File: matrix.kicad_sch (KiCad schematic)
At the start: 285 parts, among them SW2 SW_SPDT, SW3 SW_SPDT

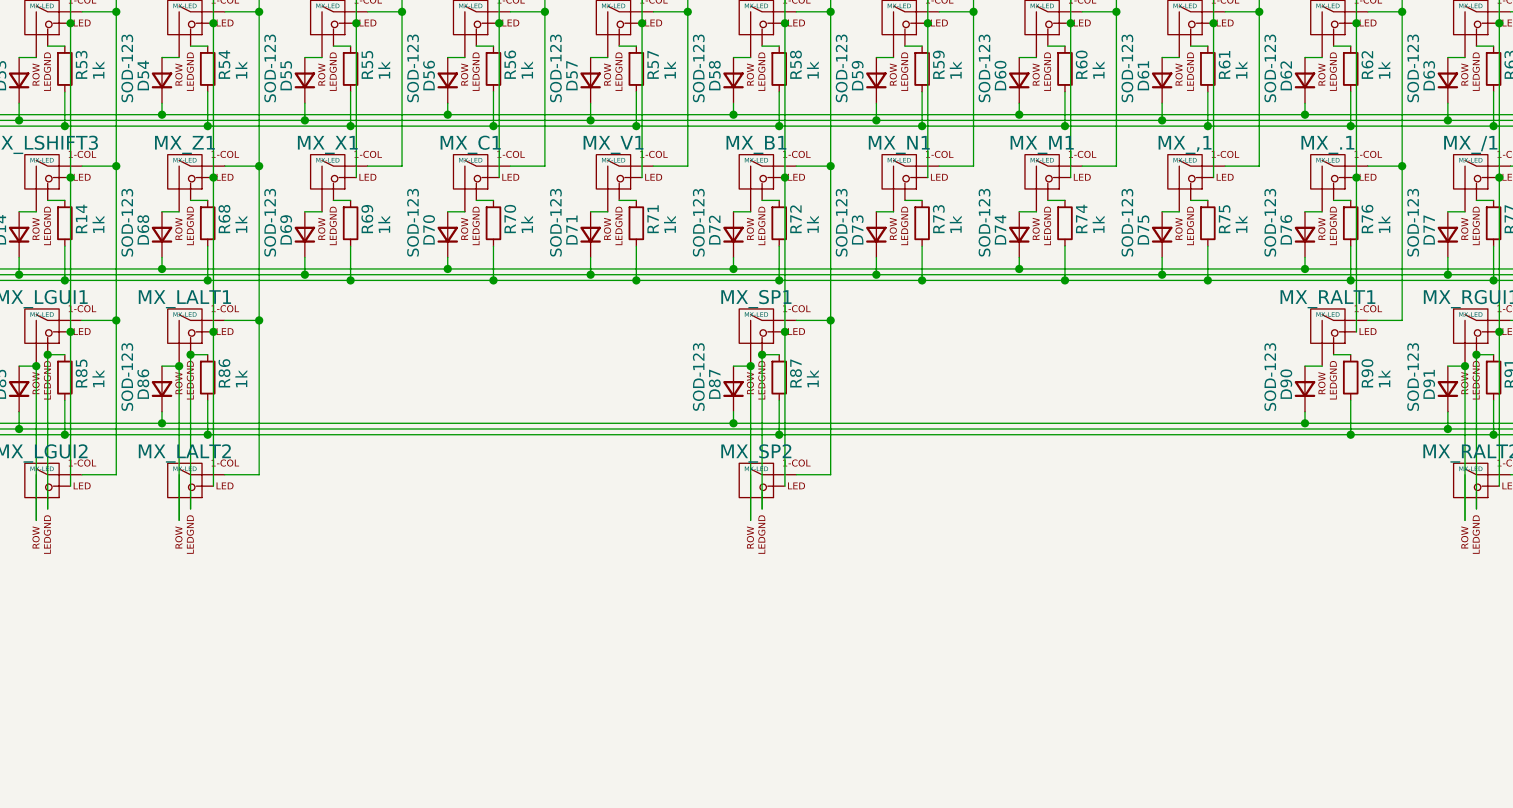
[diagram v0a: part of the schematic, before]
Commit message: Added 3U and 10U footprints to the PCB
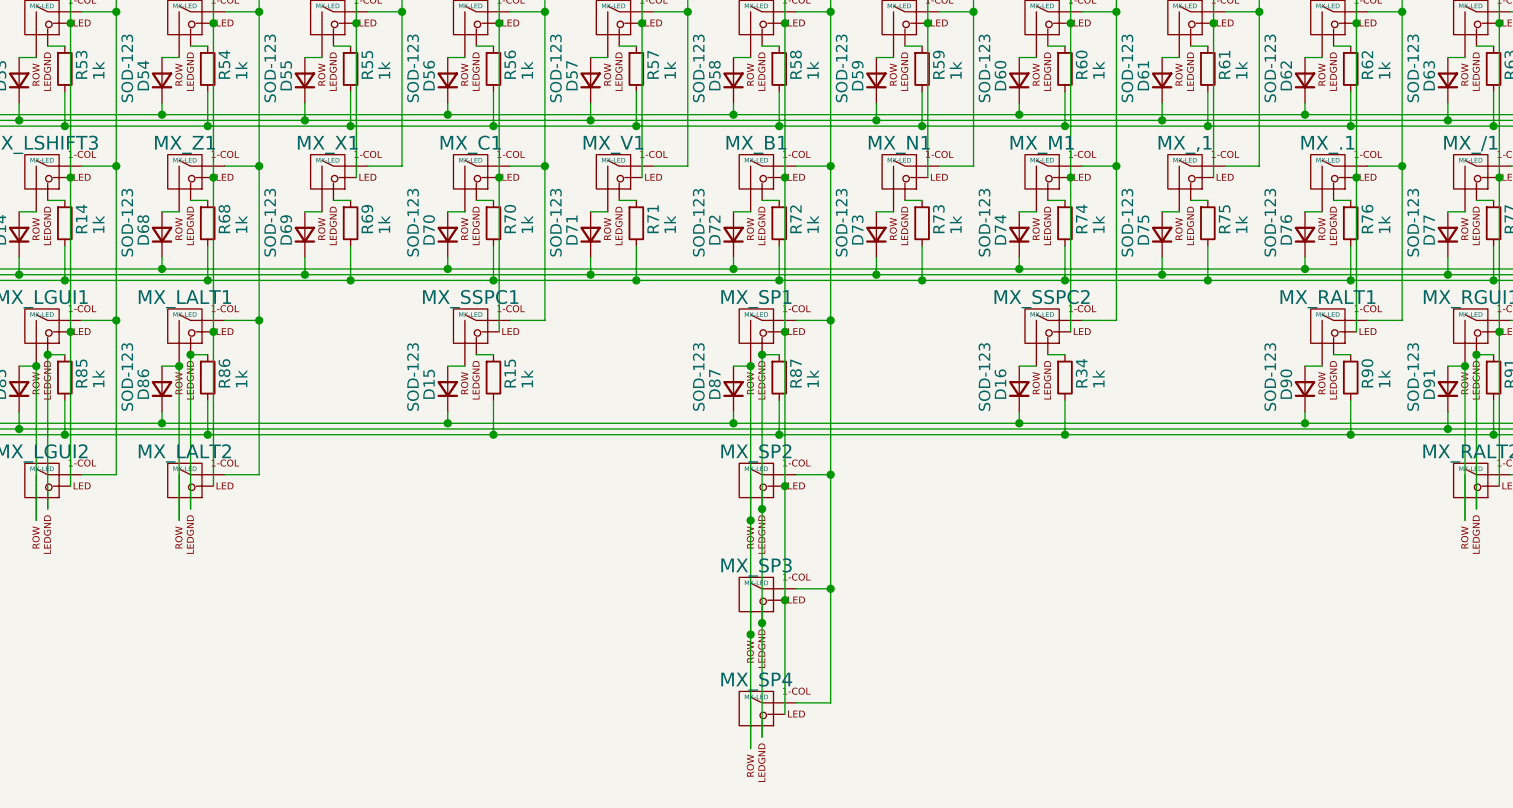
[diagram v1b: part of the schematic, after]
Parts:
- added D15, D16: SOD-123, KBD8X_MK2_Components:D_SOD-123, symbol KBD8X_MK2_Components:D_Small
- added MX_SP3: MX-LED, KBD8X_MK2_Switches:MXOnly-10U-ReversedStabilizers, symbol KBD8X_MK2_Switches:MX-LED
- added MX_SP4: MX-LED, KBD8X_MK2_Switches:MXOnly-1U, symbol KBD8X_MK2_Switches:MX-LED
- added MX_SSPC1, MX_SSPC2: MX-LED, KBD8X_MK2_Switches:MXOnly-3U-ReversedStabilizers, symbol KBD8X_MK2_Switches:MX-LED
- added R15, R34: 1k, KBD8X_MK2_Components:R_0603, symbol KBD8X_MK2_Components:R_Small
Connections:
- net +5V: now also MX_SP3.3 (LED), MX_SP4.3 (LED), MX_SSPC1.3 (LED), MX_SSPC2.3 (LED)
- net COL2: now also MX_SSPC1.1 (COL)
- net COL3: now also MX_SP3.1 (COL), MX_SP4.1 (COL)
- net COL4: now also MX_SSPC2.1 (COL)
- net LEDGND: now also R15.2, R34.2
- net ROW10: now also D15.1 (K), D16.1 (K)
- net at D87.2 (A), MX_SP1.2 (ROW), MX_SP2.2 (ROW): now also MX_SP3.2 (ROW), MX_SP4.2 (ROW)
- net at MX_SP1.4 (LEDGND), MX_SP2.4 (LEDGND), R87.1: now also MX_SP3.4 (LEDGND), MX_SP4.4 (LEDGND)
- new net: D16.2 (A), MX_SSPC2.2 (ROW)
- new net: MX_SSPC2.4 (LEDGND), R34.1
- new net: D15.2 (A), MX_SSPC1.2 (ROW)
- new net: MX_SSPC1.4 (LEDGND), R15.1
